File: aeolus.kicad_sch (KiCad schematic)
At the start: 59 parts, among them J1 Barrel_Jack_Switch, J2 Conn_01x04_Pin, J3 Conn_01x04_Pin, J4 Conn_01x04_Pin, J5 Conn_01x04_Pin, J6 Conn_01x04_Pin, Q1 2N3904, U1 XIAO-ESP32-C6-SMD, U2 MPM3610GQV-P, U3 LM66100DCK, U4 EMC2101-ACZL-TR, U6 74LVC3G07, U7 INA238

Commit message: refactor: update Qwiic connector CAD model and footprint
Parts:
- removed J5, J6: Conn_01x04_Pin, Aeolus:JST BM04B-SRSS-TB(LF)(SN)_4xP1.00mm, symbol Connector:Conn_01x04_Pin
- added G1: qwiic_Logo, symbol Qwiic_Logo:qwiic_Logo
- added J5, J6: Conn_01x04_MountingPin, Aeolus:JST BM04B-SRSS-TB(LF)(SN)_4xP1.00mm, symbol Connector_Generic_MountingPin:Conn_01x04_MountingPin
- J1: renamed from J2; now fitted
- J2: renamed from J3; now fitted
- J3: renamed from J4; now fitted
- J4: renamed from J1; now fitted
- Q1: now fitted
- renumbered C11 to C10, C8 to C11, C6 to C12, C9 to C6, C12 to C8, C10 to C9, R4 to R1, R15 to R10, R9 to R11, R13 to R12, R14 to R13, R16 to R14, R8 to R15, R5 to R3, R3 to R4, R1 to R5, R10 to R6, R11 to R7, R7 to R8, R6 to R9, TP2 to TP1, TP8 to TP10, TP3 to TP2, TP1 to TP3, TP10 to TP5, TP9 to TP6, TP5 to TP7, TP6 to TP8, TP7 to TP9, U2 to U1, U3 to U2, U1 to U3, U7 to U4, U6 to U5, U4 to U6
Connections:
- net +3V3: now also J5.2 (Pin_2), J6.2 (Pin_2)
- net GND: now also J5.1 (Pin_1), J5.MP (MountPin), J6.1 (Pin_1), J6.MP (MountPin)
- net SCL: now also J5.4 (Pin_4), J6.4 (Pin_4)
- net SDA: now also J5.3 (Pin_3), J6.3 (Pin_3)
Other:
- note added: "1.2A Out Max More than enough for the ESP32"
- note added: "12V DC Barrel In - Center + Fuse is 4A Continuous TVS for Transient and ESD Suppression"
- note added: "12V to 5V Buck"
- note added: "3+1 Fan Headers Fan PWM is split buffered from the fan controller Tach 1 goes to fan controller Tachs 2 and 3 goes to ESP for monitoring"
- note added: "ESP32 5V Backpower Prevention"
- note added: "ESP32-C6 Built in Wifi/BT/Zigbee Antenna Powered via 5V Buck to the 5V pin Ideal Diode used to be prevent backfeeding the 5V rail"
- note added: "ESP32-C6 XIAO"
- note added: "Fan Controller and Temperature Sensor"
- note added: "Fan Current and Voltage Monitoring"
- note added: "Fan Headers"
- note added: "Fan PWM Distribution"
- note added: "Fan Power Monitoring Shunt 7m Ohm LSB is 152.59uA Address can be configured to 0x40, 0x41, 0x43, 0x44"
- note added: "Ideal Diode Max output is 1.5A ESP shouldn't draw more than 500mA"
- note added: "Mounting Holes"
- note added: "Power Status LEDs"
- note added: "Qwiic Connectors"
- note added: "Qwiic compatible conntectors to allow for fan controller modification or upgrades"
- note added: "Sized for M3 screws to attach to the enclosure"
- note added: "The fan controller has only one PWM output but a bank of 9 120mm fans could draw up to 4A in order to not melt the wires and reduce voltage drop the header has been split into 3 to allow for reduced currents running through the fan wires Using the buffers to distribute the PWM signal prevents signal degridation and ensures clean signals to reach each bank of fans"
- note added: "Transistor is wired up to act as a diode The fan controller uses the current running through it to determine temperature of the external environement"
- moved on the sheet: C1, C10, C11, C12, C2, C3, C4, C5, C6, C7, C8, C9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

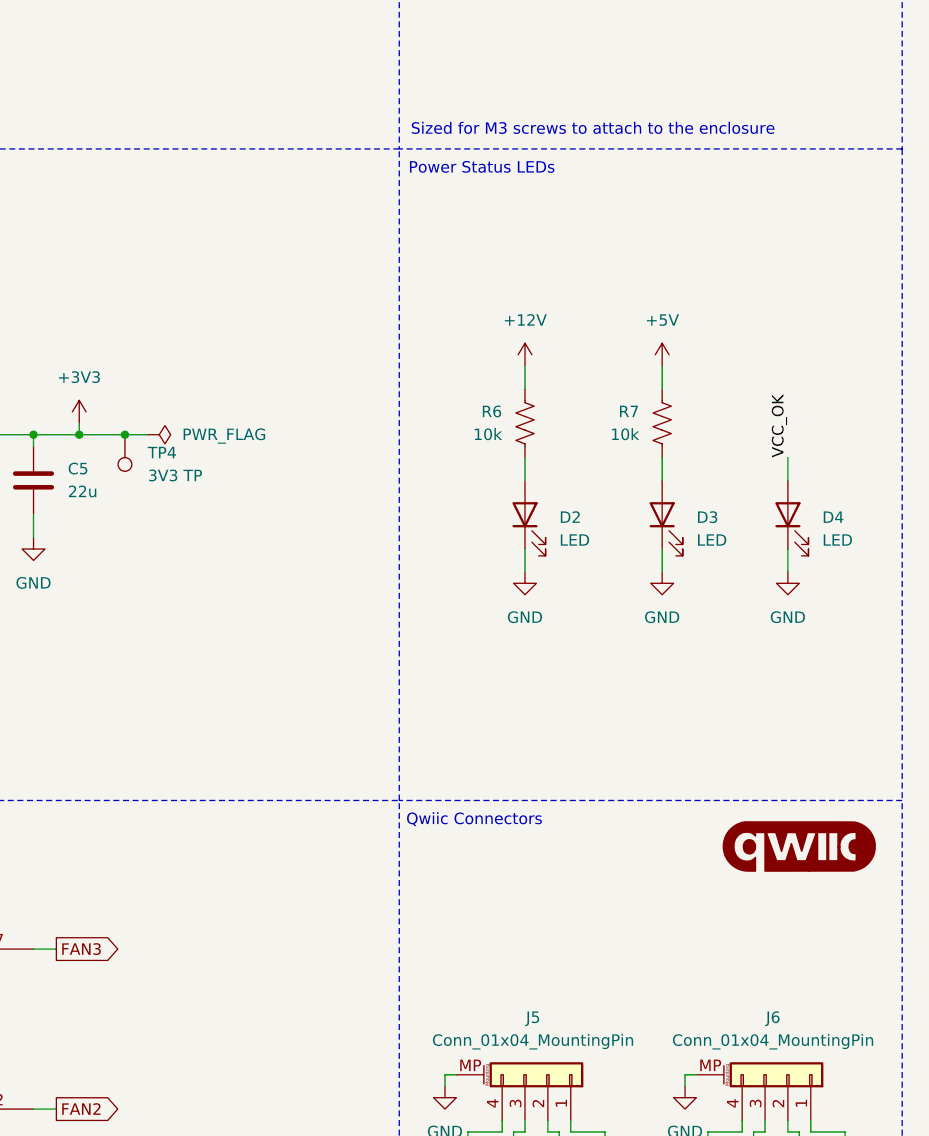
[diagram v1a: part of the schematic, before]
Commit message: style: added OSHW and Qwiic Logos to PCB and Schematic
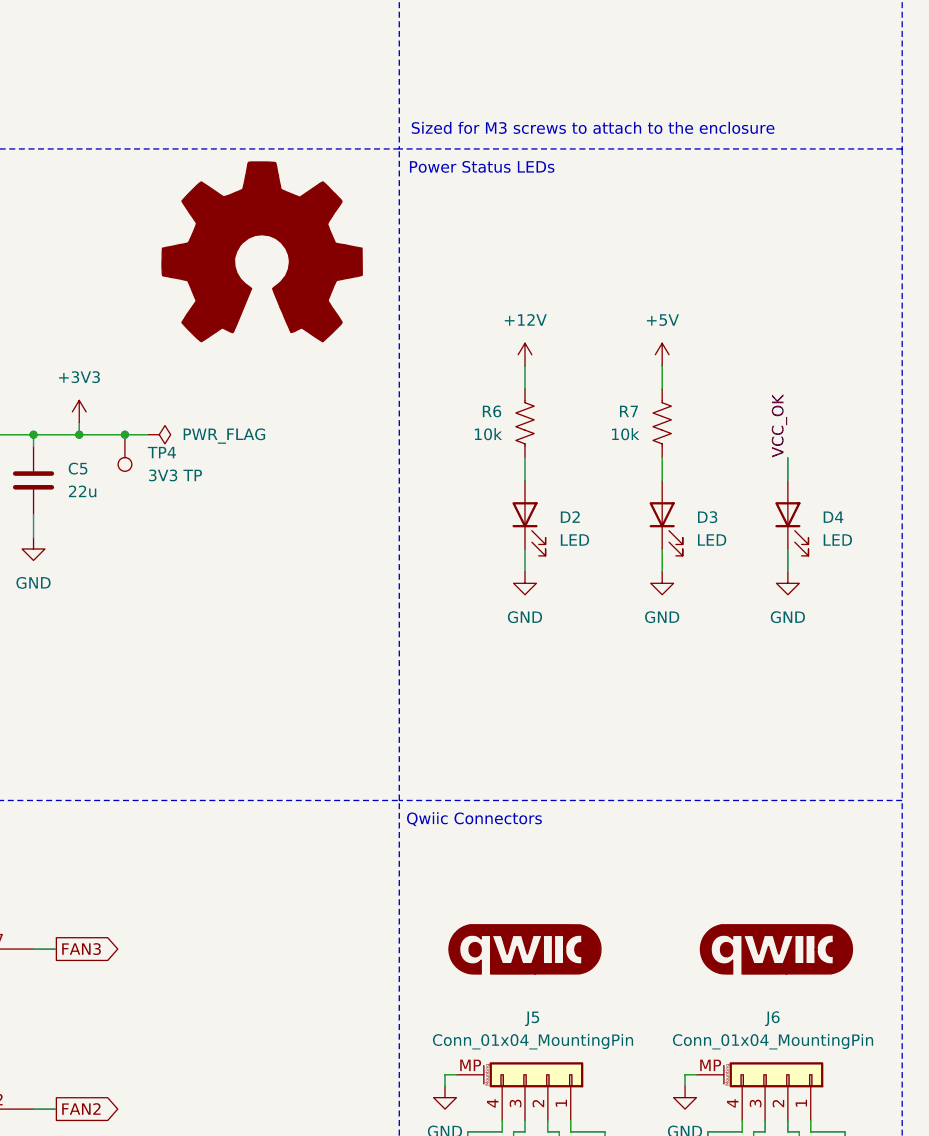
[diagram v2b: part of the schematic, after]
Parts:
- added G2: qwiic_Logo, Qwiic_Logo:qwiic_5.5mm, symbol Qwiic_Logo:qwiic_Logo
- G1: footprint (none) -> Qwiic_Logo:qwiic_5.5mm
- J5, J6: MPN (none) -> BM04B-SRSS-TB(LF)(SN)
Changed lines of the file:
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@@
 			)
 		)
+		(property "MPN" "BM04B-SRSS-TB(LF)(SN)"
+			(at 368.3 184.15 0)
+			(effects
+				(font
+					(size 1.27 1.27)
+				)
+				(hide yes)
+			)
+		)
 		(pin "2"
 		)
@@
 	)
 	(symbol
+		(lib_id "Qwiic_Logo:qwiic_Logo")
+		(at 365.76 170.18 0)
+		(unit 1)
+		(exclude_from_sim no)
+		(in_bom yes)
+		(on_board no)
+		(dnp no)
+		(fields_autoplaced yes)
+		(property "Reference" "G2"
+			(at 365.76 166.37 0)
+			(effects
+				(font
+					(size 1.27 1.27)
+				)
+				(hide yes)
+			)
+		)
+		(property "Value" "qwiic_Logo"
+			(at 365.76 173.99 0)
+			(effects
+				(font
+					(size 1.27 1.27)
+				)
+				(hide yes)
+			)
+		)
+		(property "Footprint" "Qwiic_Logo:qwiic_5.5mm"
+			(at 365.76 176.53 0)
+			(effects
+				(font
+					(size 1.27 1.27)
+				)
+				(hide yes)
+			)
+		)
+		(property "Datasheet" ""
+			(at 365.76 170.18 0)
+			(effects
+				(font
+					(size 1.27 1.27)
+				)
+				(hide yes)
+			)
+		)
+		(property "Description" ""
+			(at 365.76 170.18 0)
+			(effects
+				(font
+					(size 1.27 1.27)
+				)
+				(hide yes)
+			)
+		)
+		(instances
+			(project ""
+				(path "/9fcef582-88b0-445f-9371-37d79a145b84"
+					(reference "G2")
+					(unit 1)
+				)
+			)
+		)
+	)
+	(symbol
 		(lib_id "power:GND")
 		(at 314.96 46.99 0)
@@
 	)
 	(symbol
+		(lib_id "Graphic:Logo_Open_Hardware_Large")
+		(at 336.55 93.98 0)
+		(unit 1)
+		(exclude_from_sim no)
+		(in_bom no)
+		(on_board no)
+		(dnp no)
+		(fields_autoplaced yes)
+		(property "Reference" "#SYM1"
+			(at 336.55 81.28 0)
+			(effects
+				(font
+					(size 1.27 1.27)
+				)
+				(hide yes)
+			)
+		)
+		(property "Value" "Logo_Open_Hardware_Large"
+			(at 336.55 104.14 0)
+			(effects
+				(font
+					(size 1.27 1.27)
+				)
+				(hide yes)
+			)
+		)
+		(property "Footprint" "Symbol:OSHW-Symbol_6.7x6mm_SilkScreen"
+			(at 336.55 93.98 0)
+			(effects
+				(font
+					(size 1.27 1.27)
+				)
+				(hide yes)
+			)
+		)
+		(property "Datasheet" "~"
+			(at 336.55 93.98 0)
+			(effects
+				(font
+					(size 1.27 1.27)
+				)
+				(hide yes)
+			)
+		)
+		(property "Description" "Open Hardware logo, large"
+			(at 336.55 93.98 0)
+			(effects
+				(font
+					(size 1.27 1.27)
+				)
+				(hide yes)
+			)
+		)
+		(property "Sim.Enable" "0"
+			(at 336.55 93.98 0)
+			(effects
+				(font
+					(size 1.27 1.27)
+				)
+				(hide yes)
+			)
+		)
+		(instances
+			(project ""
+				(path "/9fcef582-88b0-445f-9371-37d79a145b84"
+					(reference "#SYM1")
+					(unit 1)
+				)
+			)
+		)
+	)
+	(symbol
 		(lib_id "Device:LED")
 		(at 381 121.92 90)
@@
 	(symbol
 		(lib_id "Qwiic_Logo:qwiic_Logo")
-		(at 396.24 158.75 0)
+		(at 393.7 170.18 0)
 		(unit 1)
 		(exclude_from_sim no)
@@
 		(fields_autoplaced yes)
 		(property "Reference" "G1"
-			(at 396.24 154.94 0)
+			(at 393.7 166.37 0)
 			(effects
 				(font
@@
 		)
 		(property "Value" "qwiic_Logo"
-			(at 396.24 162.56 0)
+			(at 393.7 173.99 0)
 			(effects
 				(font
@@
 			)
 		)
-		(property "Footprint" ""
-			(at 396.24 165.1 0)
+		(property "Footprint" "Qwiic_Logo:qwiic_5.5mm"
+			(at 393.7 176.53 0)
 			(effects
 				(font
@@
 		)
 		(property "Datasheet" ""
-			(at 396.24 158.75 0)
+			(at 393.7 170.18 0)
 			(effects
 				(font
@@
 		)
 		(property "Description" ""
-			(at 396.24 158.75 0)
+			(at 393.7 170.18 0)
 			(effects
 				(font
@@
 			(at 394.97 184.15 0)
 			(effects
+				(font
+					(size 1.27 1.27)
+				)
+				(hide yes)
+			)
+		)
+		(property "MPN" "BM04B-SRSS-TB(LF)(SN)"
+			(at 394.97 184.15 0)
+			(effects
